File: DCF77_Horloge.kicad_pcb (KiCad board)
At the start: 4 copper layers, 50 parts, among them J1 USB_B_Micro, J2 Conn_SWD, J3 Conn_Display, J4 Conn_DCF, J5 GPIO, Q1 AO3401A, SW1 RST, SW2 Boot, U1 MCP73831-2-OT, U2 NCP1117-3.3_SOT223, U3 RP2040, U4 W25Q128JVS, Y1 ABLS-12.000MHZ-B4-T

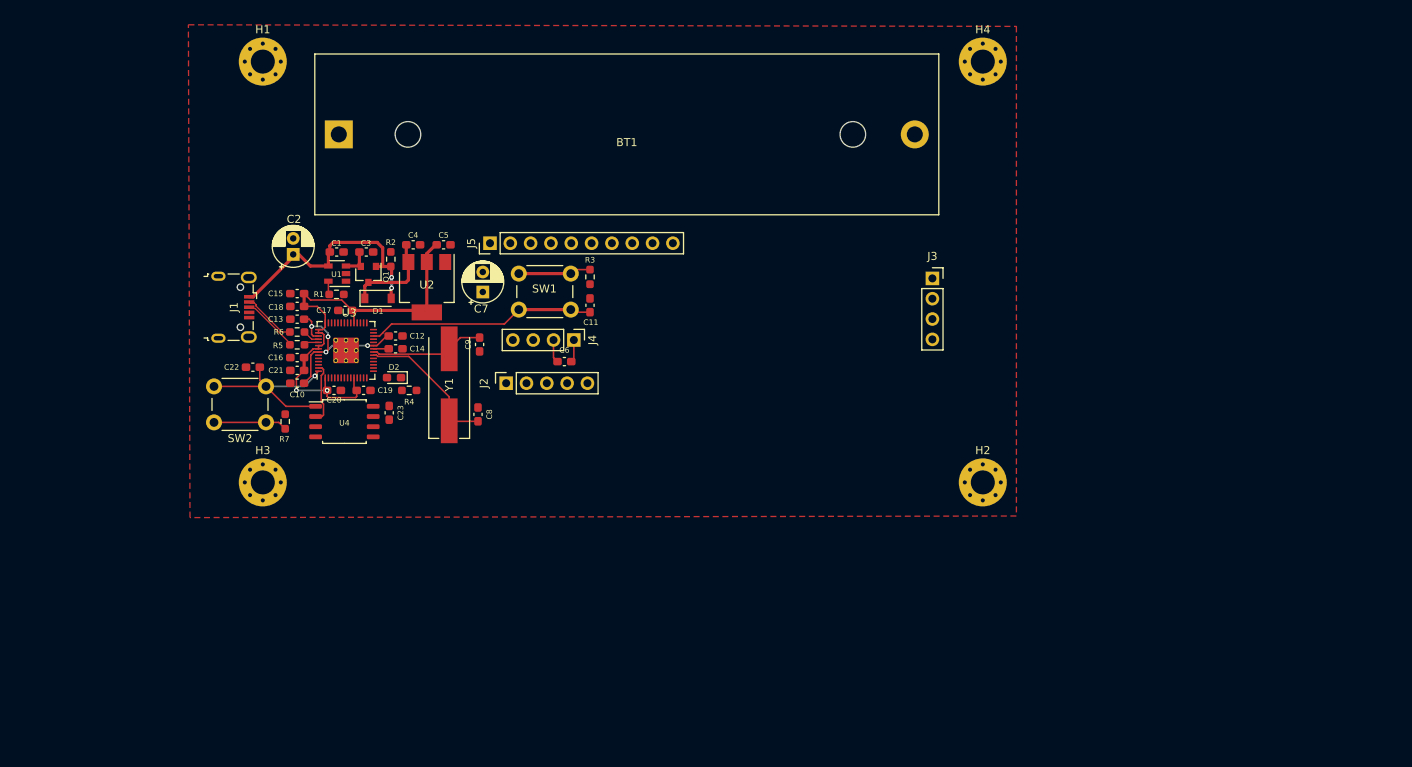
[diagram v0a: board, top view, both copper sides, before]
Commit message: Add pull up for i2c and change layout
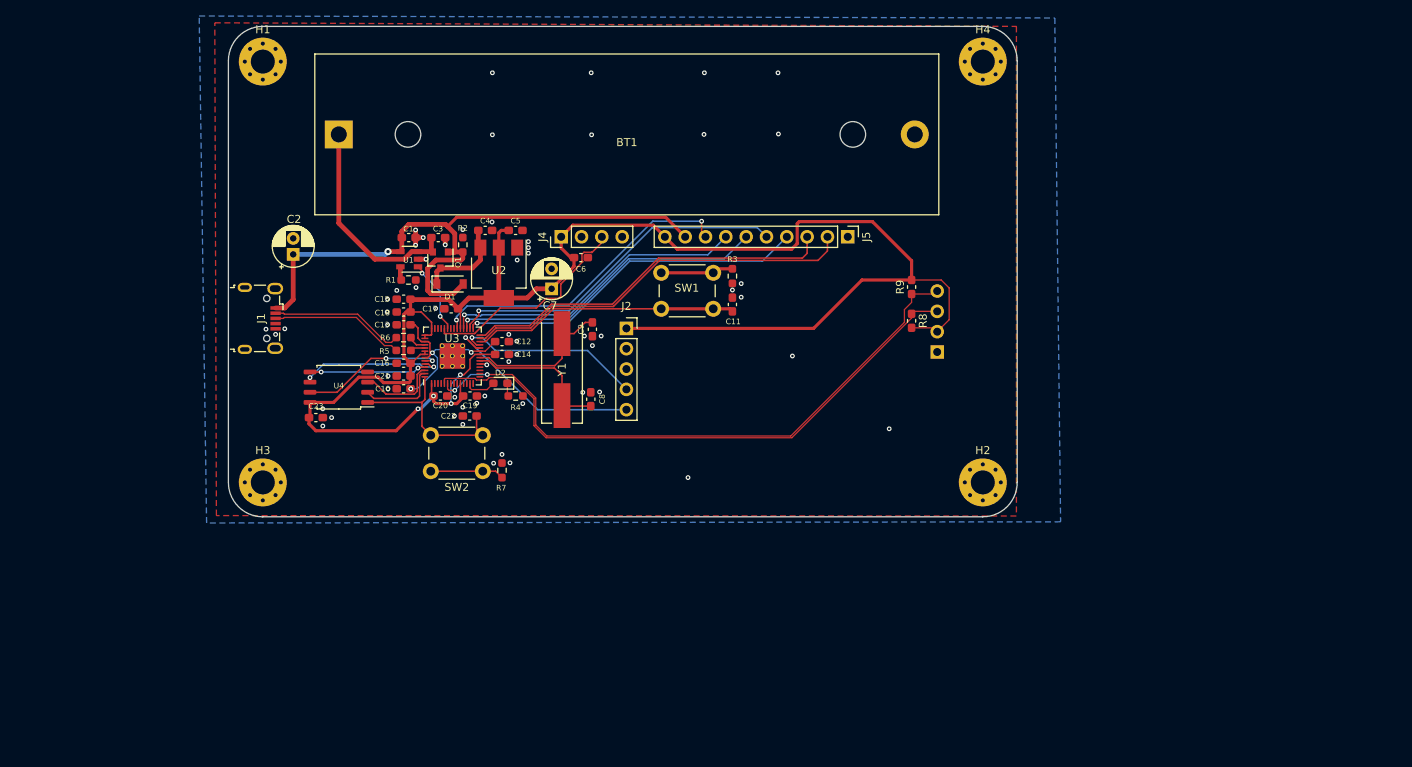
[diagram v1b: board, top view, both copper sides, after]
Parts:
- added R8: 2K, Resistor_SMD:R_0603_1608Metric_Pad1.05x0.95mm_HandSolder, F.Cu at (185.1, 65.8)
- added R9: 2K, Resistor_SMD:R_0603_1608Metric_Pad1.05x0.95mm_HandSolder, F.Cu at (185.1, 61.6)
- J3: moved to B.Cu
- moved J5 44.7 mm to (177.1, 55.3), turned to 270 degrees
- moved C22 27.8 mm to (129.9, 77.7)
- moved R7 27.8 mm to (133.9, 84.5)
- moved SW2 27.8 mm to (131.5, 84.6)
- moved SW1 17.8 mm to (153.8, 59.8)
- moved C11 17.8 mm to (162.7, 63.8)
- moved R3 17.8 mm to (162.7, 60.2)
- moved J2 16.5 mm to (149.4, 66.8), turned to 0 degrees
- moved Y1 14.2 mm to (141.4, 71.9)
- moved C8 14.2 mm to (145.0, 75.6)
- moved C9 14.2 mm to (145.2, 66.9)
- moved C12 13.3 mm to (133.9, 68.4)
- moved C14 13.3 mm to (133.9, 70.0)
- moved C19 13.3 mm to (129.9, 75.2)
- moved C10 13.3 mm to (121.6, 74.3)
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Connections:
- J1 pad 4: (no net) -> Net-(J1-Pad4)
- J2 pad 2: (no net) -> Net-(J2-Pad2)
- J2 pad 3: (no net) -> RST
- J5 pad 1: /MCU/GPIO15 -> GND
- J5 pad 10: /MCU/GPIO24 -> +3V3
- J5 pad 9: /MCU/GPIO23 -> +5V
- U3 pad 11: (no net) -> Net-(U3-Pad11)
- U3 pad 12: (no net) -> Net-(U3-Pad12)
- U3 pad 14: (no net) -> Net-(U3-Pad14)
- U3 pad 15: (no net) -> Net-(U3-Pad15)
- U3 pad 16: (no net) -> Net-(U3-Pad16)
- U3 pad 17: (no net) -> Net-(U3-Pad17)
- U3 pad 18: /MCU/GPIO15 -> Net-(U3-Pad18)
- U3 pad 2: STATUS_BAT -> Net-(U3-Pad2)
- U3 pad 3: (no net) -> Net-(U3-Pad3)
- U3 pad 35: /MCU/GPIO23 -> Net-(U3-Pad35)
- U3 pad 36: /MCU/GPIO24 -> Net-(U3-Pad36)
- U3 pad 37: (no net) -> STATUS_BAT
- U3 pad 39: (no net) -> Net-(U3-Pad39)
- U3 pad 4: (no net) -> Net-(U3-Pad4)
- U3 pad 40: (no net) -> Net-(U3-Pad40)
- U3 pad 41: (no net) -> Net-(U3-Pad41)
- U3 pad 7: (no net) -> Net-(U3-Pad7)
- U3 pad 8: (no net) -> Net-(U3-Pad8)
- U3 pad 9: (no net) -> Net-(U3-Pad9)
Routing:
- net +3V3: track 61.7 -> 219.5 mm, vias 2 -> 4
- net SDA: track 0.00 -> 77.0 mm, vias 0 -> 2
- net SCL: track 0.00 -> 74.3 mm
- net +5V: track 30.8 -> 81.2 mm, vias 2 -> 1
- net /MCU/GPIO16: track 0.00 -> 49.7 mm
- net /MCU/GPIO17: track 0.00 -> 47.2 mm
- net /MCU/GPIO18: track 0.00 -> 44.2 mm, vias 0 -> 1
- net /MCU/GPIO19: track 0.00 -> 43.4 mm, vias 0 -> 1
- net /MCU/GPIO20: track 0.00 -> 40.2 mm, vias 0 -> 1
- net /MCU/GPIO22: track 0.00 -> 39.3 mm, vias 0 -> 2
- net /MCU/GPIO21: track 0.00 -> 38.6 mm, vias 0 -> 1
- net DCF: track 0.00 -> 27.4 mm
- net SWCL: track 0.00 -> 26.2 mm, vias 0 -> 1
- net SWDO: track 0.00 -> 23.5 mm, vias 0 -> 1
- net +BATT: track 3.74 -> 27.0 mm
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- added copper zone on B.Cu, net GND
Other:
- board outline added: 98.6 x 61.3 mm
- copper layers 4 -> 2

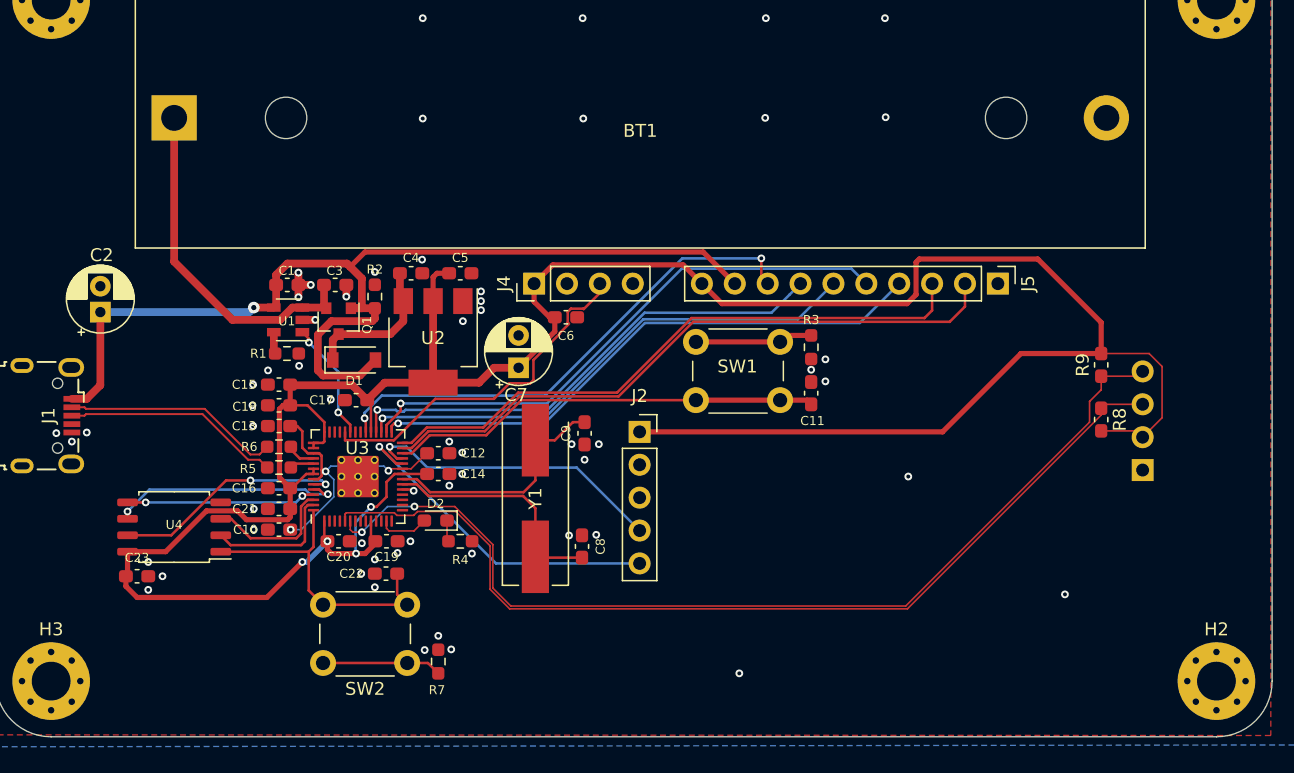
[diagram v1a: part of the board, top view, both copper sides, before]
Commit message: change MCU from RP2040 to ESP32-WROOM-32
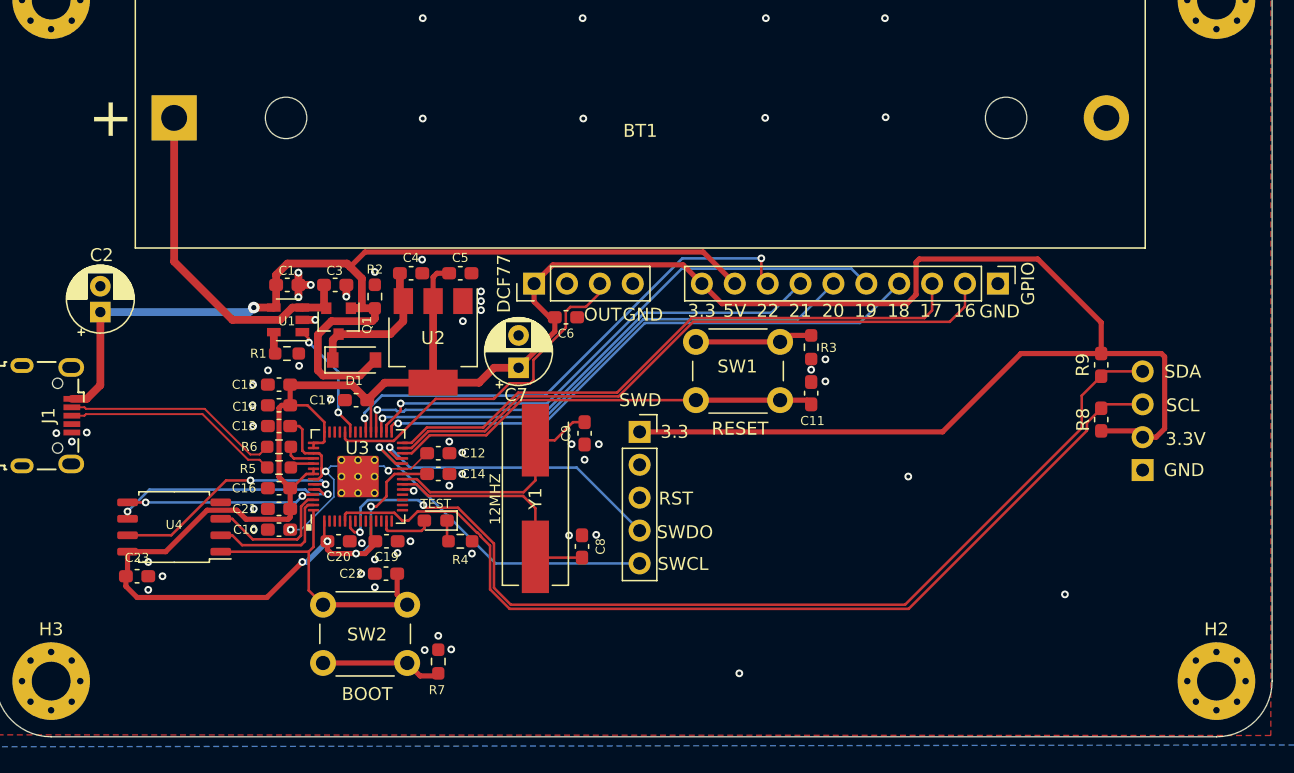
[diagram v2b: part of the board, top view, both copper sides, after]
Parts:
- renumbered J4 to DCF77, J5 to GPIO, J2 to SWD, D2 to TEST
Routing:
- net +3V3: track 219.5 -> 221.1 mm
- net SDA: track 77.0 -> 78.2 mm
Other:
- board text added: "+"
- board text added: "."
- board text added: "12MHZ"
- board text added: "16"
- board text added: "17"
- board text added: "18"
- board text added: "19"
- board text added: "20"
- board text added: "21"
- board text added: "22"
- board text added: "3.3"
- board text added: "3.3V"
- board text added: "5V"
- board text added: "BOOT"
- board text added: "GND"
- board text added: "OUT"
- board text added: "RESET"
- board text added: "RST"
- board text added: "SCL"
- board text added: "SDA"
- board text added: "SWCL"
- board text added: "SWDO"

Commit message: some changes
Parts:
- removed C11, C12, C14, C16, C17, C18, C19, C20, C21, C22, C23: 100nF, Capacitor_SMD:C_0603_1608Metric_Pad1.08x0.95mm_HandSolder
- removed C13, C15: 1uF, Capacitor_SMD:C_0603_1608Metric_Pad1.08x0.95mm_HandSolder
- removed DCF77: Conn_DCF, Connector_PinHeader_2.54mm:PinHeader_1x04_P2.54mm_Vertical
- removed GPIO: GPIO, Connector_PinHeader_2.54mm:PinHeader_1x10_P2.54mm_Vertical
- removed SWD: Conn_SWD, Connector_PinSocket_2.54mm:PinSocket_1x05_P2.54mm_Vertical
- removed TEST: test, LED_SMD:LED_0603_1608Metric_Pad1.05x0.95mm_HandSolder
- removed U4: W25Q128JVS, Package_SO:SOIC-8_5.23x5.23mm_P1.27mm
- removed Y1: ABLS-12.000MHZ-B4-T, RP2040_minimal:Crystal_SMD_HC49-US
- C10: value 100nF -> 0.1uF
- C6: value 10uF -> 0.1uF
- C8: value 27pF -> 10uF
- C9: value 27pF -> 0.1uF
- J1: value USB_B_Micro -> USB_C_Receptacle_USB2.0; footprint Connector_USB:USB_Micro-B_Wuerth_629105150521 -> Connector_USB:USB_C_Receptacle_GCT_USB4085; moved to B.Cu
- R4: value 520 -> 560
- R5: value 27 -> 10k
- R6: value 27 -> 5k1
- R7: value 10k -> 5k1
- SW1: footprint Button_Switch_THT:SW_PUSH_6mm_H5mm -> Button_Switch_SMD:SW_SPST_FSMSM
- SW2: value Boot -> boot; footprint Button_Switch_THT:SW_PUSH_6mm_H5mm -> Button_Switch_SMD:SW_SPST_FSMSM
- U3: value RP2040 -> ESP32-S2-WROVER; footprint RP2040_minimal:RP2040-QFN-56 -> RF_Module:ESP32-S2-WROVER
- moved J1 90.1 mm to (192.3, 49.6)
- moved R6 71.9 mm to (192.9, 58.7)
- moved R7 70.3 mm to (193.0, 46.5), turned to 180 degrees
- moved C2 57.2 mm to (164.8, 62.0)
- moved R3 54.7 mm to (108.0, 58.2), turned to 180 degrees
- moved C9 39.3 mm to (108.0, 79.5), turned to 0 degrees
- moved C8 37.5 mm to (108.0, 81.1), turned to 0 degrees
- moved C6 26.9 mm to (147.5, 84.5), turned to 270 degrees
- moved SW1 25.0 mm to (156.2, 84.7)
- moved C1 18.9 mm to (141.1, 55.8)
- moved Q1 18.9 mm to (145.1, 58.5)
- moved U1 18.9 mm to (141.2, 58.5)
- moved C3 18.9 mm to (144.8, 55.8)
- moved C4 18.9 mm to (150.7, 54.9)
- moved C5 18.9 mm to (154.4, 54.9)
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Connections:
- C10 pad 1: +1V1 -> GND
- C10 pad 2: GND -> /BOOT
- C6 pad 2: +3V3 -> Net-(C6-Pad2)
- C8 pad 2: Net-(C8-Pad2) -> +3V3
- C9 pad 2: Net-(C9-Pad2) -> +3V3
- R3 pad 1: Net-(R3-Pad1) -> /RST
- R3 pad 2: GND -> +3V3
- R4 pad 1: GND -> Net-(C6-Pad2)
- R4 pad 2: Net-(D2-Pad1) -> /RST
- R5 pad 1: USB+ -> /BOOT
- R5 pad 2: Net-(R5-Pad2) -> +3V3
- R6 pad 1: USB- -> GND
- R6 pad 2: Net-(R6-Pad2) -> Net-(J1-PadB5)
- R7 pad 1: Net-(R7-Pad1) -> GND
- R7 pad 2: GND -> Net-(J1-PadA5)
- SW1 pad 1: Net-(R3-Pad1) -> Net-(C6-Pad2)
- SW1 pad 2: Net-(C11-Pad1) -> GND
- SW2 pad 1: Net-(R7-Pad1) -> GND
- SW2 pad 2: /MCU/QSPI_SS -> /BOOT
- U3 pad 1: +3V3 -> GND
- U3 pad 10: +3V3 -> Net-(U3-Pad10)
- U3 pad 19: GND -> Net-(U3-Pad19)
- U3 pad 2: Net-(U3-Pad2) -> +3V3
- U3 pad 20: Net-(C8-Pad2) -> Net-(U3-Pad20)
- U3 pad 21: Net-(C9-Pad2) -> Net-(U3-Pad21)
- U3 pad 22: +3V3 -> USB-
- U3 pad 23: +1V1 -> USB+
- U3 pad 24: SWCL -> Net-(U3-Pad24)
- U3 pad 25: SWDO -> Net-(U3-Pad25)
- U3 pad 26: Net-(C11-Pad1) -> GND
- U3 pad 27: /MCU/GPIO16 -> Net-(U3-Pad27)
- U3 pad 28: /MCU/GPIO17 -> Net-(U3-Pad28)
- U3 pad 29: /MCU/GPIO18 -> Net-(U3-Pad29)
- U3 pad 3: Net-(U3-Pad3) -> /BOOT
- U3 pad 30: /MCU/GPIO19 -> Net-(U3-Pad30)
- U3 pad 31: /MCU/GPIO20 -> Net-(U3-Pad31)
- U3 pad 32: /MCU/GPIO21 -> Net-(U3-Pad32)
- U3 pad 33: +3V3 -> SCL
- U3 pad 34: /MCU/GPIO22 -> Net-(U3-Pad34)
- U3 pad 36: Net-(U3-Pad36) -> SDA
- U3 pad 37: STATUS_BAT -> Net-(U3-Pad37)
- U3 pad 38: DCF -> Net-(U3-Pad38)
- U3 pad 41: Net-(U3-Pad41) -> /RST
- U3 pad 42: +3V3 -> GND
- U3 pad 43: +3V3 -> GND
- U3 pad 5: SCL -> Net-(U3-Pad5)
- U3 pad 6: SDA -> Net-(U3-Pad6)
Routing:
- net +3V3: track 221.1 -> 82.3 mm, vias 4 -> 2
- net USB-: track 16.8 -> 69.9 mm
- net USB+: track 16.8 -> 69.9 mm
- net /RST: track 0.00 -> 52.7 mm
- net /MCU/GPIO16: track 49.7 -> 0.00 mm
- net /MCU/GPIO17: track 47.2 -> 0.00 mm
- net /MCU/GPIO18: track 44.2 -> 0.00 mm, vias 1 -> 0
- net /MCU/GPIO19: track 43.4 -> 0.00 mm, vias 1 -> 0
- net /MCU/GPIO20: track 40.2 -> 0.00 mm, vias 1 -> 0
- net /MCU/GPIO22: track 39.3 -> 0.00 mm, vias 2 -> 0
- net /MCU/GPIO21: track 38.6 -> 0.00 mm, vias 1 -> 0
- net Net-(C11-Pad1): track 33.4 -> 0.00 mm
- net DCF: track 27.4 -> 0.00 mm
- net SWCL: track 26.1 -> 0.00 mm, vias 1 -> 0
- net /MCU/QSPI_SS: track 23.9 -> 0.00 mm
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- added copper zone on F.Cu, net +BATT
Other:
- board text removed: "12MHZ"
- board text removed: "16"
- board text removed: "17"
- board text removed: "18"
- board text removed: "19"
- board text removed: "20"
- board text removed: "21"
- board text removed: "22"
- board text removed: "3.3"
- board text removed: "5V"
- board text removed: "BOOT"
- board text removed: "OUT"
- board text removed: "RESET"
- board text removed: "RST"
- board text removed: "SWCL"
- board text removed: "SWDO"
